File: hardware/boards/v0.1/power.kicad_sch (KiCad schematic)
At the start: 50 parts, among them IC3 SP3401-02UTG, J2 USB, SW26 POWER, U20 TPS62A02DRL, U23 BQ21040DBV, U31 FUSB302B01MPX, U32 LTC2942, U36 STM6601CQ2DDM6x

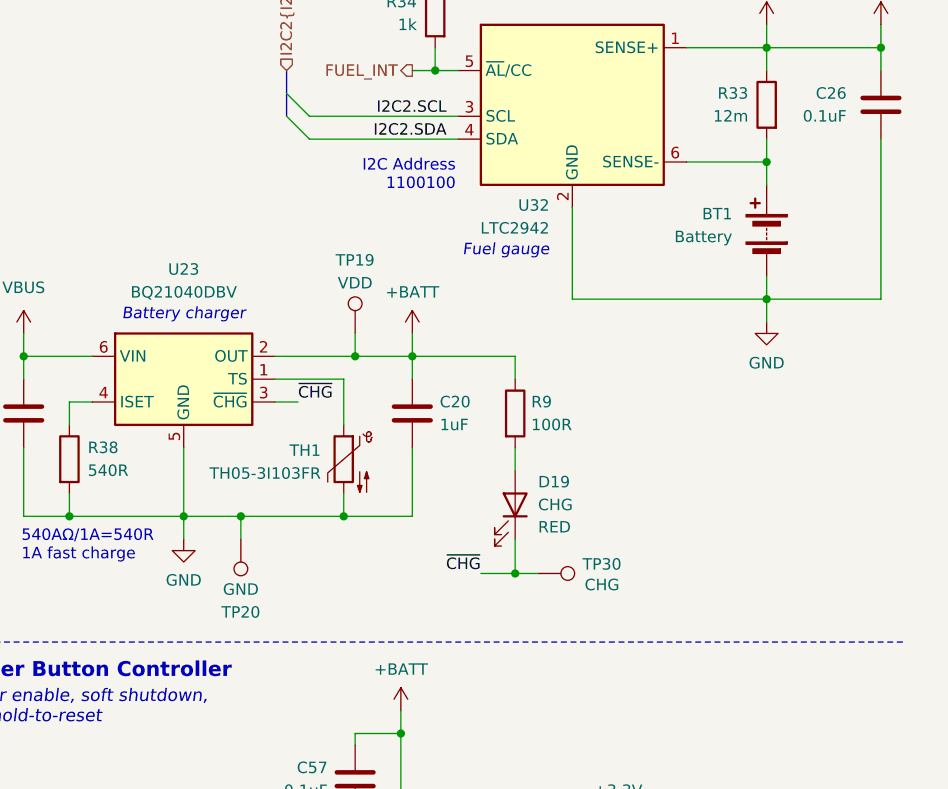
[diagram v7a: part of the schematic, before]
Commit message: feat: add more test points
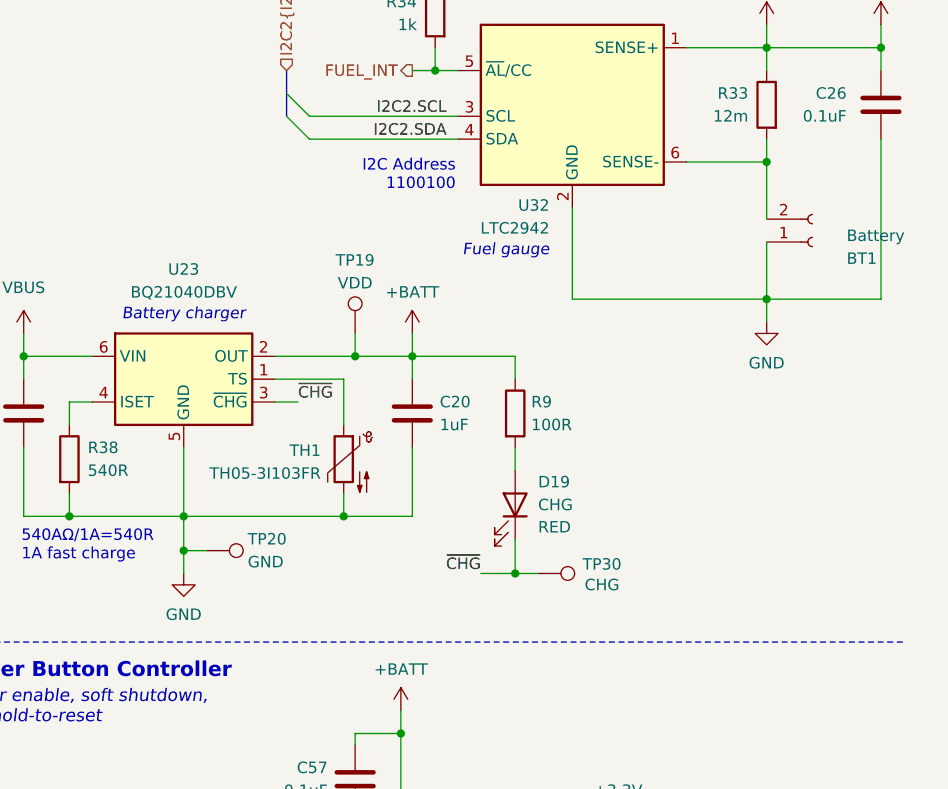
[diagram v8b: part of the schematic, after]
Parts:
- BT1: symbol Device:Battery -> Connector:Conn_01x02_Socket
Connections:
- net GND: now also BT1.1 (Pin_1); no longer BT1.2 (-)
- net at R33.2, U32.6 (SENSE-): now also BT1.2 (Pin_2); no longer BT1.1 (+)
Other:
- moved on the sheet: TP20
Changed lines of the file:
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@@
 	)
 	(junction
+		(at 204.47 87.63)
+		(diameter 0)
+		(color 0 0 0 0)
+	)
+	(junction
 		(at 241.3 90.17)
 		(diameter 0)
@@
 	)
 	(junction
-		(at 210.82 83.82)
-		(diameter 0)
-		(color 0 0 0 0)
-	)
-	(junction
 		(at 67.31 153.67)
 		(diameter 0)
@@
 	(wire
 		(pts
+			(xy 204.47 87.63) (xy 207.01 87.63)
+		)
+		(stroke
+			(width 0)
+			(type default)
+		)
+	)
+	(wire
+		(pts
 			(xy 78.74 153.67) (xy 76.2 153.67)
 		)
@@
 	(wire
 		(pts
+			(xy 204.47 87.63) (xy 204.47 90.17)
+		)
+		(stroke
+			(width 0)
+			(type default)
+		)
+	)
+	(wire
+		(pts
 			(xy 214.63 66.04) (xy 223.52 66.04)
 		)
@@
 	(wire
 		(pts
-			(xy 204.47 83.82) (xy 210.82 83.82)
+			(xy 204.47 83.82) (xy 222.25 83.82)
 		)
 		(stroke
@@
 	(wire
 		(pts
-			(xy 269.24 57.15) (xy 269.24 59.69)
+			(xy 269.24 53.34) (xy 269.24 59.69)
 		)
 		(stroke
@@
 	(wire
 		(pts
-			(xy 204.47 83.82) (xy 204.47 86.36)
+			(xy 204.47 83.82) (xy 204.47 87.63)
 		)
 		(stroke
@@
 	(wire
 		(pts
-			(xy 210.82 83.82) (xy 222.25 83.82)
-		)
-		(stroke
-			(width 0)
-			(type default)
-		)
-	)
-	(wire
-		(pts
 			(xy 49.53 156.21) (xy 44.45 156.21)
 		)
@@
 	(wire
 		(pts
-			(xy 269.24 44.45) (xy 269.24 46.99)
-		)
-		(stroke
-			(width 0)
-			(type default)
-		)
-	)
-	(wire
-		(pts
-			(xy 210.82 83.82) (xy 210.82 86.36)
+			(xy 269.24 44.45) (xy 269.24 50.8)
 		)
 		(stroke
@@
 	(symbol
 		(lib_id "Connector:TestPoint")
-		(at 210.82 86.36 180)
+		(at 207.01 87.63 270)
 		(unit 1)
 		(exclude_from_sim no)
@@
 		(dnp no)
 		(property "Reference" "TP20"
-			(at 210.82 94.488 0)
+			(at 211.582 86.36 90)
 			(effects
 				(font
 					(size 1.27 1.27)
 				)
+				(justify left)
 			)
 		)
 		(property "Value" "GND"
-			(at 210.82 91.948 0)
+			(at 211.582 88.9 90)
 			(effects
 				(font
 					(size 1.27 1.27)
 				)
+				(justify left)
 			)
 		)
 		(property "Footprint" "TestPoint:TestPoint_Pad_D1.0mm"
-			(at 205.74 86.36 0)
+			(at 207.01 92.71 0)
 			(effects
 				(font
@@
 		)
 		(property "Datasheet" "~"
-			(at 205.74 86.36 0)
+			(at 207.01 92.71 0)
 			(effects
 				(font
@@
 		)
 		(property "Description" "test point"
-			(at 210.82 86.36 0)
+			(at 207.01 87.63 0)
 			(effects
 				(font
@@
 		)
 		(property "Arrow Part Number" ""
-			(at 210.82 86.36 0)
+			(at 207.01 87.63 0)
 			(effects
 				(font
@@
 		)
 		(property "Arrow Price/Stock" ""
-			(at 210.82 86.36 0)
+			(at 207.01 87.63 0)
 			(effects
 				(font
@@
 		)
 		(property "MANUFACTURER" ""
-			(at 210.82 86.36 0)
+			(at 207.01 87.63 0)
 			(effects
 				(font
@@
 		)
 		(property "MAXIMUM_PACKAGE_HEIGHT" ""
-			(at 210.82 86.36 0)
+			(at 207.01 87.63 0)
 			(effects
 				(font
@@
 		)
 		(property "PARTREV" ""
-			(at 210.82 86.36 0)
+			(at 207.01 87.63 0)
 			(effects
 				(font
@@
 		)
 		(property "STANDARD" ""
-			(at 210.82 86.36 0)
+			(at 207.01 87.63 0)
 			(effects
 				(font
@@
 		)
 		(property "Connector" ""
-			(at 210.82 86.36 0)
+			(at 207.01 87.63 0)
 			(effects
 				(font
@@
 	(symbol
 		(lib_id "power:GND")
-		(at 204.47 86.36 0)
+		(at 204.47 90.17 0)
 		(unit 1)
 		(exclude_from_sim no)
@@
 		(dnp no)
 		(property "Reference" "#PWR076"
-			(at 204.47 92.71 0)
+			(at 204.47 96.52 0)
 			(effects
 				(font
@@
 		)
 		(property "Value" "GND"
-			(at 204.47 90.932 0)
+			(at 204.47 94.742 0)
 			(effects
 				(font
@@
 		)
 		(property "Footprint" ""
-			(at 204.47 86.36 0)
+			(at 204.47 90.17 0)
 			(effects
 				(font
@@
 		)
 		(property "Datasheet" ""
-			(at 204.47 86.36 0)
+			(at 204.47 90.17 0)
 			(effects
 				(font
@@
 		)
 		(property "Description" "Power symbol creates a global label with name \"GND\" , ground"
-			(at 204.47 86.36 0)
+			(at 204.47 90.17 0)
 			(effects
 				(font
@@
 	)
 	(symbol
-		(lib_id "Device:Battery")
-		(at 269.24 52.07 0)
-		(mirror y)
+		(lib_id "Connector:Conn_01x02_Socket")
+		(at 274.32 53.34 0)
+		(mirror x)
 		(unit 1)
 		(exclude_from_sim no)
@@
 		(dnp no)
 		(property "Reference" "BT1"
-			(at 265.43 50.2284 0)
+			(at 278.13 55.1816 0)
 			(effects
 				(font
@@
 		)
 		(property "Value" "Battery"
-			(at 265.43 52.7684 0)
+			(at 278.13 52.6416 0)
 			(effects
 				(font
@@
 		)
 		(property "Footprint" "Connector_JST:JST_PH_S2B-PH-SM4-TB_1x02-1MP_P2.00mm_Horizontal"
-			(at 269.24 50.546 90)
+			(at 274.32 53.34 0)
 			(effects
 				(font
@@
 		)
 		(property "Datasheet" "~"
-			(at 269.24 50.546 90)
+			(at 274.32 53.34 0)
 			(effects
 				(font
@@
 			)
 		)
-		(property "Description" "Multiple-cell battery"
-			(at 269.24 52.07 0)
+		(property "Description" "Generic connector, single row, 01x02, script generated"
+			(at 274.32 53.34 0)
 			(effects
 				(font
@@
 		)
 		(property "Arrow Part Number" ""
-			(at 269.24 52.07 0)
+			(at 274.32 53.34 0)
 			(effects
 				(font
@@
 		)
 		(property "Arrow Price/Stock" ""
-			(at 269.24 52.07 0)
+			(at 274.32 53.34 0)
 			(effects
 				(font
@@
 		)
 		(property "MANUFACTURER" ""
-			(at 269.24 52.07 0)
+			(at 274.32 53.34 0)
 			(effects
 				(font
@@
 		)
 		(property "MAXIMUM_PACKAGE_HEIGHT" ""
-			(at 269.24 52.07 0)
+			(at 274.32 53.34 0)
 			(effects
 				(font
@@
 		)
 		(property "PARTREV" ""
-			(at 269.24 52.07 0)
+			(at 274.32 53.34 0)
 			(effects
 				(font
@@
 		)
 		(property "STANDARD" ""
-			(at 269.24 52.07 0)
+			(at 274.32 53.34 0)
 			(effects
 				(font
@@
 		)
 		(property "Connector" ""
-			(at 269.24 52.07 0)
+			(at 274.32 53.34 0)
 			(effects
 				(font
